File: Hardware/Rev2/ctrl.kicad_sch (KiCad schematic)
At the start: 36 parts, among them J1 USB_C_Receptacle_USB2.0_16P, J2 Conn_01x08, SW1 SW_Push, SW2 SW_Push, U12 74LS125, U13 74LS125, U14 74LS125, U15 ESP32-S3-WROOM-1, U16 USBLC6-2SC6, U17 XC6220B331MR

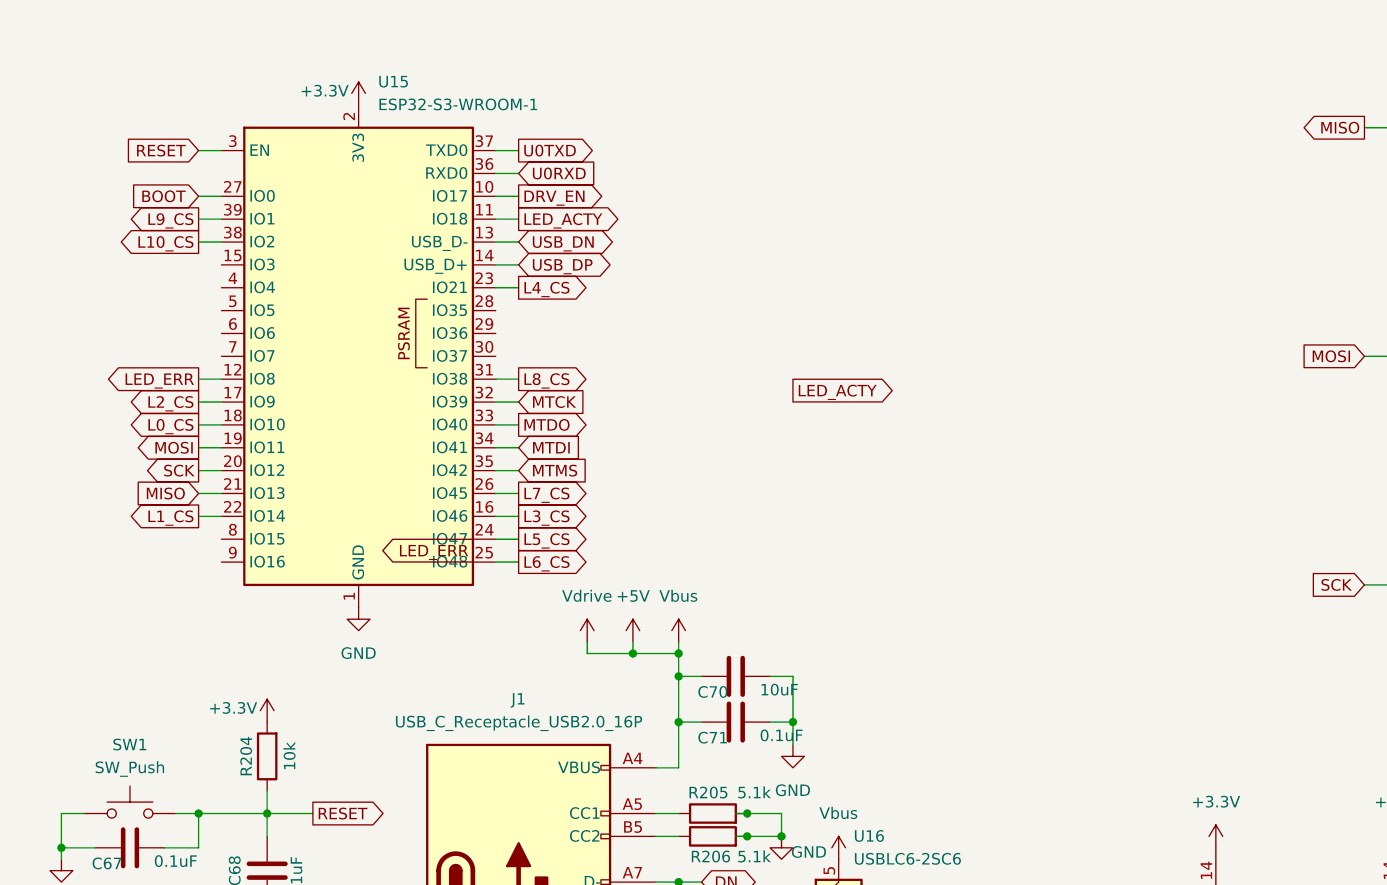
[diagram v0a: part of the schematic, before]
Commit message: add SD card for future expansion
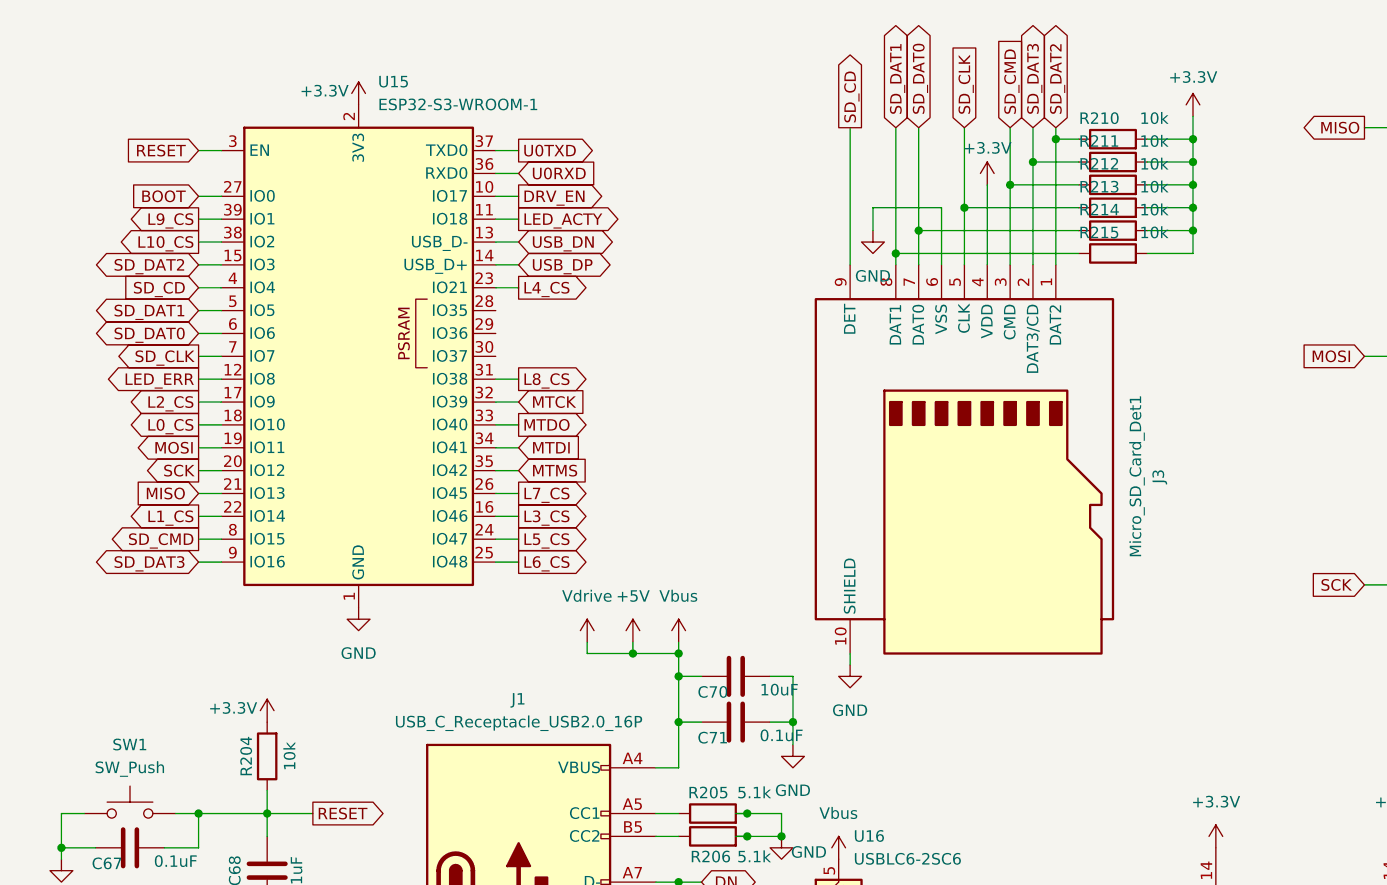
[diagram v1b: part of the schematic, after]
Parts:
- added J3: Micro_SD_Card_Det1, custom_footprints:TFW11-N1S1-2000-A, symbol Connector:Micro_SD_Card_Det1
- added R210, R211, R212, R213, R214, R215: 10k, Resistor_SMD:R_0603_1608Metric_Pad0.98x0.95mm_HandSolder, symbol Device:R
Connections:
- net +3.3V: now also J3.4 (VDD), R210.2, R211.2, R212.2, R213.2, R214.2, R215.2
- net GND: now also J3.10 (SHIELD), J3.6 (VSS)
- net SD_DAT2: now reaches U15.15 (IO3)
- net SD_DAT2: now also J3.1 (DAT2), R210.1
- net SD_CD: now reaches U15.4 (IO4)
- net SD_CD: now also J3.9 (DET)
- net SD_DAT1: now reaches U15.5 (IO5)
- net SD_DAT1: now also J3.8 (DAT1), R215.1
- net SD_DAT0: now reaches U15.6 (IO6)
- net SD_DAT0: now also J3.7 (DAT0), R214.1
- net SD_CLK: now reaches U15.7 (IO7)
- net SD_CLK: now also J3.5 (CLK), R213.1
- net SD_CMD: now reaches U15.8 (IO15)
- net SD_CMD: now also J3.3 (CMD), R212.1
- net SD_DAT3: now reaches U15.9 (IO16)
- net SD_DAT3: now also J3.2 (DAT3/CD), R211.1

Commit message: add power LED
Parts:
- added D736: LED, LED_SMD:LED_1206_3216Metric_Pad1.42x1.75mm_HandSolder, symbol Device:LED
- added R216: 220R, Resistor_SMD:R_0603_1608Metric_Pad0.98x0.95mm_HandSolder, symbol Device:R
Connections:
- net +3.3V: now also R216.1
- net GND: now also D736.1 (K)
- new net: D736.2 (A), R216.2

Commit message: add 3D models, and change USB-C connector type
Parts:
- J1: footprint custom_footprints:TPS16-N1F1-2016-A -> custom_footprints:ShouHan-USBC-16P-2MD; MPN C52750323 -> C2765186
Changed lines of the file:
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@@
 			)
 		)
-		(property "Footprint" "custom_footprints:TPS16-N1F1-2016-A"
+		(property "Footprint" "custom_footprints:ShouHan-USBC-16P-2MD"
 			(at 72.39 111.76 0)
 			(effects
@@
 			)
 		)
-		(property "MPN" "C52750323"
+		(property "MPN" "C2765186"
 			(at 68.58 111.76 0)
 			(effects

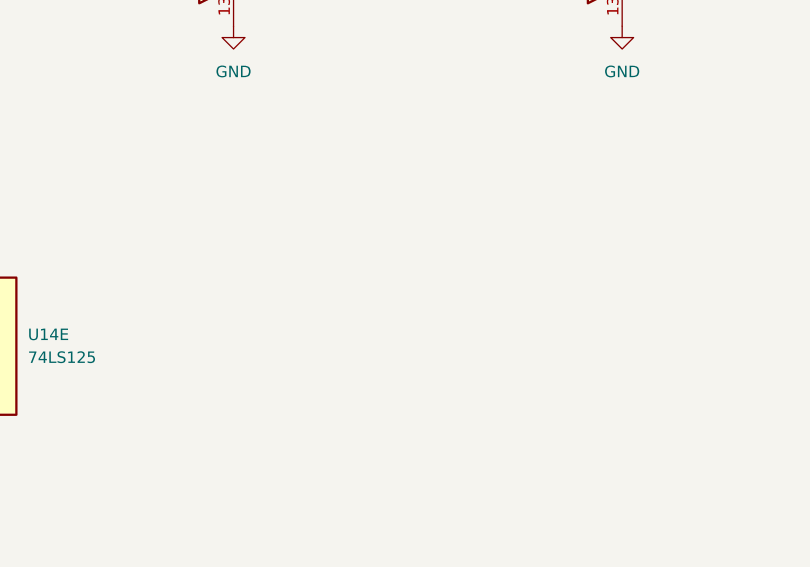
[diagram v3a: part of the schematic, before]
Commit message: add header for SD card pins
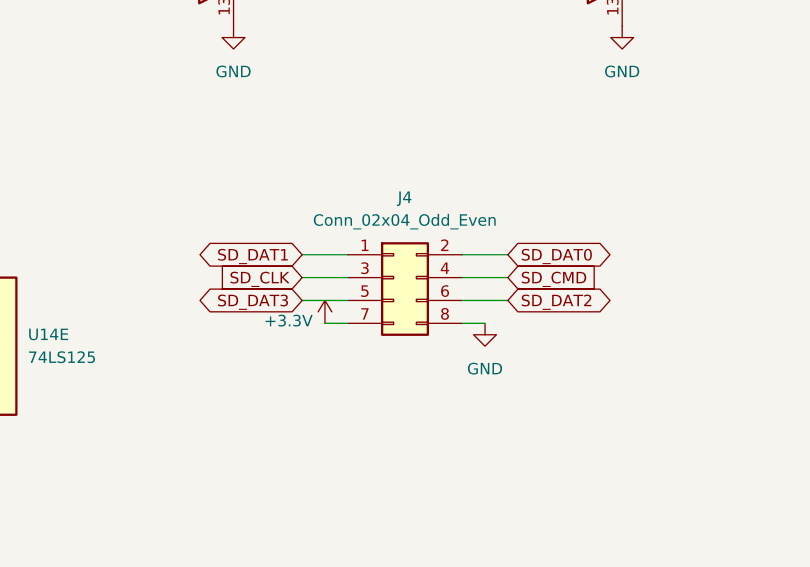
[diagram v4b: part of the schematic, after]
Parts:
- added J4: Conn_02x04_Odd_Even, Connector_PinHeader_2.54mm:PinHeader_2x04_P2.54mm_Vertical, symbol Connector_Generic:Conn_02x04_Odd_Even
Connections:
- net +3.3V: now also J4.7 (Pin_7)
- net GND: now also J4.8 (Pin_8)
- net SD_CLK: now also J4.3 (Pin_3)
- net SD_CMD: now also J4.4 (Pin_4)
- net SD_DAT0: now also J4.2 (Pin_2)
- net SD_DAT1: now also J4.1 (Pin_1)
- net SD_DAT2: now also J4.6 (Pin_6)
- net SD_DAT3: now also J4.5 (Pin_5)

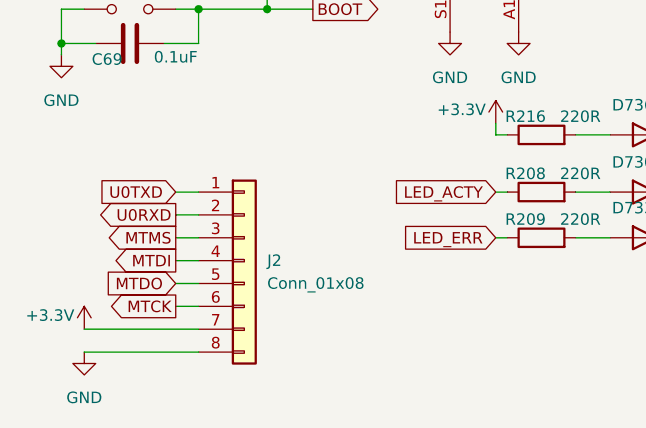
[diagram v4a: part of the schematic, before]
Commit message: add +5V rail to debug header
someone might want to power the board that way :/
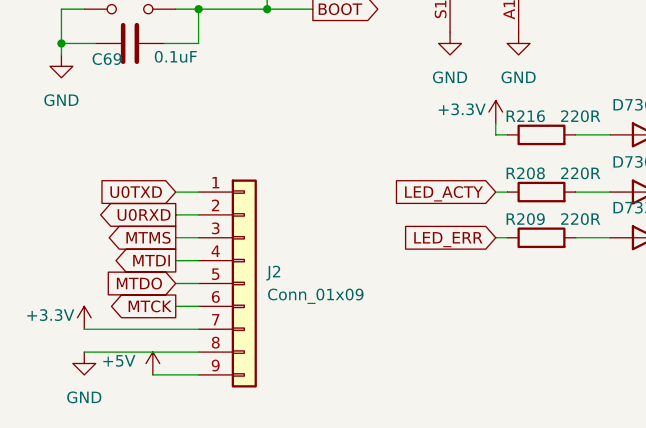
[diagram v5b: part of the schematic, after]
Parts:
- J2: value Conn_01x08 -> Conn_01x09; footprint Connector_PinHeader_2.54mm:PinHeader_1x08_P2.54mm_Vertical -> Connector_PinHeader_2.54mm:PinHeader_1x09_P2.54mm_Vertical; symbol Connector_Generic:Conn_01x08 -> Connector_Generic:Conn_01x09
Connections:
- net +5V: now also J2.9 (Pin_9)
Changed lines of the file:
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@@
 	(wire
 		(pts
-			(xy 180.34 76.2) (xy 181.61 76.2)
+			(xy 30.48 152.4) (xy 33.02 152.4)
 		)
 		(stroke
@@
 	(wire
 		(pts
-			(xy 74.93 157.48) (xy 78.74 157.48)
+			(xy 180.34 76.2) (xy 181.61 76.2)
 		)
 		(stroke
@@
 	(wire
 		(pts
-			(xy 30.48 162.56) (xy 33.02 162.56)
+			(xy 74.93 157.48) (xy 78.74 157.48)
 		)
 		(stroke
@@
 	(wire
 		(pts
-			(xy 30.48 154.94) (xy 33.02 154.94)
+			(xy 33.02 132.08) (xy 30.48 132.08)
 		)
 		(stroke
@@
 	(wire
 		(pts
-			(xy 33.02 132.08) (xy 30.48 132.08)
+			(xy 93.98 101.6) (xy 97.79 101.6)
 		)
 		(stroke
@@
 	(wire
 		(pts
-			(xy 93.98 101.6) (xy 97.79 101.6)
+			(xy 30.48 165.1) (xy 33.02 165.1)
 		)
 		(stroke
@@
 	(wire
 		(pts
+			(xy 30.48 157.48) (xy 33.02 157.48)
+		)
+		(stroke
+			(width 0)
+			(type default)
+		)
+	)
+	(wire
+		(pts
 			(xy 99.06 86.36) (xy 96.52 86.36)
 		)
@@
 	(wire
 		(pts
-			(xy 30.48 157.48) (xy 33.02 157.48)
+			(xy 20.32 132.08) (xy 17.78 132.08)
 		)
 		(stroke
@@
 	(wire
 		(pts
-			(xy 20.32 132.08) (xy 17.78 132.08)
+			(xy 152.4 152.4) (xy 157.48 152.4)
 		)
 		(stroke
@@
 	(wire
 		(pts
-			(xy 152.4 152.4) (xy 157.48 152.4)
+			(xy 223.52 113.03) (xy 228.6 113.03)
 		)
 		(stroke
@@
 	(wire
 		(pts
-			(xy 223.52 113.03) (xy 228.6 113.03)
+			(xy 33.02 38.1) (xy 35.56 38.1)
 		)
 		(stroke
@@
 	(wire
 		(pts
-			(xy 33.02 38.1) (xy 35.56 38.1)
+			(xy 149.86 152.4) (xy 152.4 152.4)
 		)
 		(stroke
@@
 	(wire
 		(pts
-			(xy 149.86 152.4) (xy 152.4 152.4)
+			(xy 20.32 170.18) (xy 33.02 170.18)
 		)
 		(stroke
@@
 	(wire
 		(pts
+			(xy 20.32 167.64) (xy 33.02 167.64)
+		)
+		(stroke
+			(width 0)
+			(type default)
+		)
+	)
+	(wire
+		(pts
 			(xy 138.43 34.29) (xy 143.51 34.29)
 		)
@@
 	(wire
 		(pts
-			(xy 30.48 165.1) (xy 33.02 165.1)
-		)
-		(stroke
-			(width 0)
-			(type default)
-		)
-	)
-	(wire
-		(pts
 			(xy 86.36 109.22) (xy 83.82 109.22)
 		)
@@
 	(wire
 		(pts
-			(xy 162.56 152.4) (xy 167.64 152.4)
+			(xy 27.94 172.72) (xy 33.02 172.72)
 		)
 		(stroke
@@
 	(wire
 		(pts
-			(xy 30.48 152.4) (xy 33.02 152.4)
+			(xy 162.56 152.4) (xy 167.64 152.4)
 		)
 		(stroke
@@
 	(wire
 		(pts
+			(xy 30.48 162.56) (xy 33.02 162.56)
+		)
+		(stroke
+			(width 0)
+			(type default)
+		)
+	)
+	(wire
+		(pts
 			(xy 66.04 55.88) (xy 68.58 55.88)
 		)
@@
 	(wire
 		(pts
-			(xy 20.32 170.18) (xy 33.02 170.18)
-		)
-		(stroke
-			(width 0)
-			(type default)
-		)
-	)
-	(wire
-		(pts
 			(xy 86.36 96.52) (xy 86.36 91.44)
 		)
@@
 	(wire
 		(pts
-			(xy 86.36 109.22) (xy 88.9 109.22)
+			(xy 30.48 160.02) (xy 33.02 160.02)
 		)
 		(stroke
@@
 	(wire
 		(pts
-			(xy 30.48 160.02) (xy 33.02 160.02)
+			(xy 86.36 109.22) (xy 88.9 109.22)
 		)
 		(stroke
@@
 	(wire
 		(pts
-			(xy 20.32 167.64) (xy 33.02 167.64)
-		)
-		(stroke
-			(width 0)
-			(type default)
-		)
-	)
-	(wire
-		(pts
 			(xy 33.02 60.96) (xy 35.56 60.96)
 		)
@@
 	(wire
 		(pts
+			(xy 30.48 154.94) (xy 33.02 154.94)
+		)
+		(stroke
+			(width 0)
+			(type default)
+		)
+	)
+	(wire
+		(pts
 			(xy 33.02 132.08) (xy 40.64 132.08)
 		)
@@
 	)
 	(symbol
-		(lib_id "Connector_Generic:Conn_01x08")
-		(at 38.1 160.02 0)
+		(lib_id "Connector_Generic:Conn_01x09")
+		(at 38.1 162.56 0)
 		(unit 1)
 		(exclude_from_sim no)
@@
 		(fields_autoplaced yes)
 		(property "Reference" "J2"
-			(at 40.64 160.0199 0)
+			(at 40.64 161.2899 0)
 			(effects
 				(font
@@
 			)
 		)
-		(property "Value" "Conn_01x08"
-			(at 40.64 162.5599 0)
+		(property "Value" "Conn_01x09"
+			(at 40.64 163.8299 0)
 			(effects
 				(font
@@
 			)
 		)
-		(property "Footprint" "Connector_PinHeader_2.54mm:PinHeader_1x08_P2.54mm_Vertical"
-			(at 38.1 160.02 0)
+		(property "Footprint" "Connector_PinHeader_2.54mm:PinHeader_1x09_P2.54mm_Vertical"
+			(at 38.1 162.56 0)
 			(effects
 				(font
@@
 		)
 		(property "Datasheet" "~"
-			(at 38.1 160.02 0)
+			(at 38.1 162.56 0)
 			(effects
 				(font
@@
 			)
 		)
-		(property "Description" "Generic connector, single row, 01x08, script generated (kicad-library-utils/schlib/autogen/connector/)"
-			(at 38.1 160.02 0)
+		(property "Description" "Generic connector, single row, 01x09, script generated (kicad-library-utils/schlib/autogen/connector/)"
+			(at 38.1 162.56 0)
 			(effects
 				(font
@@
 		)
 		(property "MPN" "C49451372"
-			(at 38.1 160.02 0)
+			(at 38.1 162.56 0)
 			(effects
 				(font
@@
 		(pin "1"
 		)
+		(pin "9"
+		)
 		(instances
 			(project ""
@@
 					(unit 1)
 				)
+			)
+		)
+	)
+	(symbol
+		(lib_id "power:+3.3V")
+		(at 27.94 172.72 0)
+		(unit 1)
+		(exclude_from_sim no)
+		(in_bom yes)
+		(on_board yes)
+		(dnp no)
+		(property "Reference" "#PWR0114"
+			(at 27.94 176.53 0)
+			(effects
+				(font
+					(size 1.27 1.27)
+				)
+				(hide yes)
+			)
+		)
+		(property "Value" "+5V"
+			(at 24.13 171.196 0)
+			(effects
+				(font
+					(size 1.27 1.27)
+				)
+			)
+		)
+		(property "Footprint" ""
+			(at 27.94 172.72 0)
+			(effects
+				(font
+					(size 1.27 1.27)
+				)
+				(hide yes)
+			)
+		)
+		(property "Datasheet" ""
+			(at 27.94 172.72 0)
+			(effects
+				(font
+					(size 1.27 1.27)
+				)
+				(hide yes)
+			)
+		)
+		(property "Description" "Power symbol creates a global label with name \"+3.3V\""
+			(at 27.94 172.72 0)
+			(effects
+				(font
+					(size 1.27 1.27)
+				)
+				(hide yes)
+			)
+		)
+		(pin "1"
+		)
+		(instances
+			(project "Rev2"
+				(path "/179c1fb3-28fd-4881-8d54-9aff58c09fe4/a439bf26-855a-431e-bb37-b656be58d856"
+					(reference "#PWR0114")
+					(unit 1)
+				)

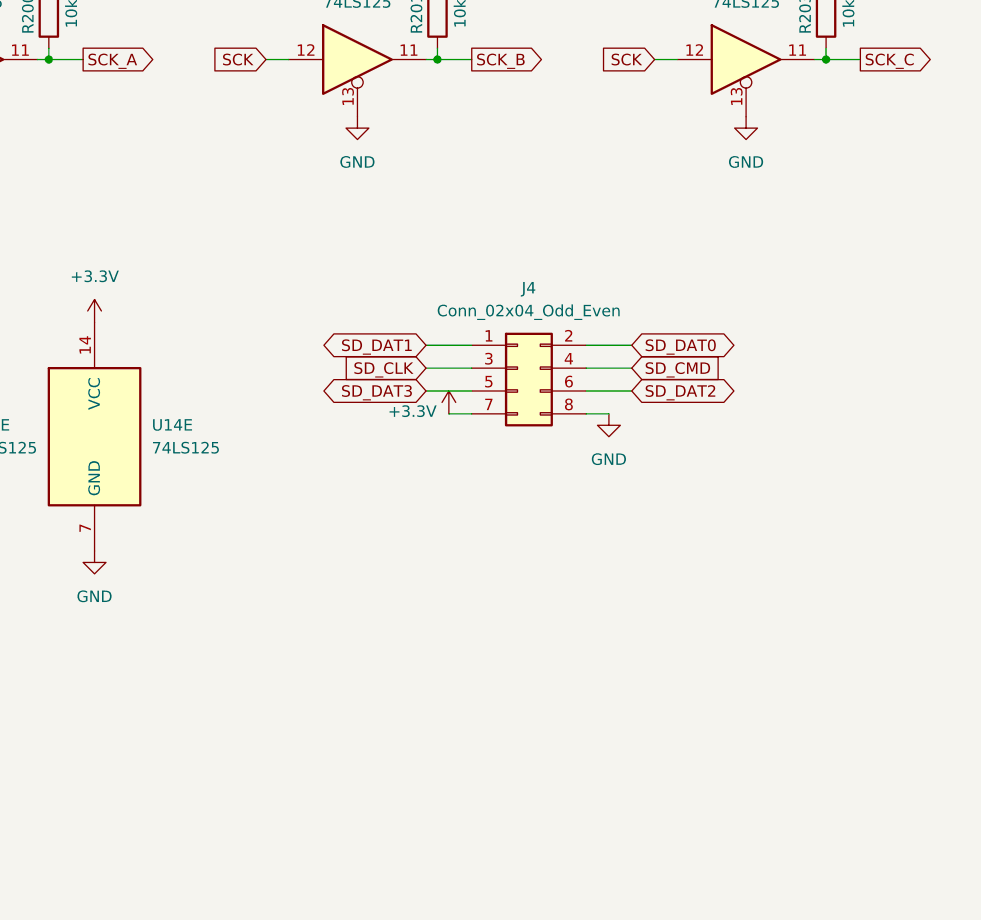
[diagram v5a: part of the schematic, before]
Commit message: add OLED display
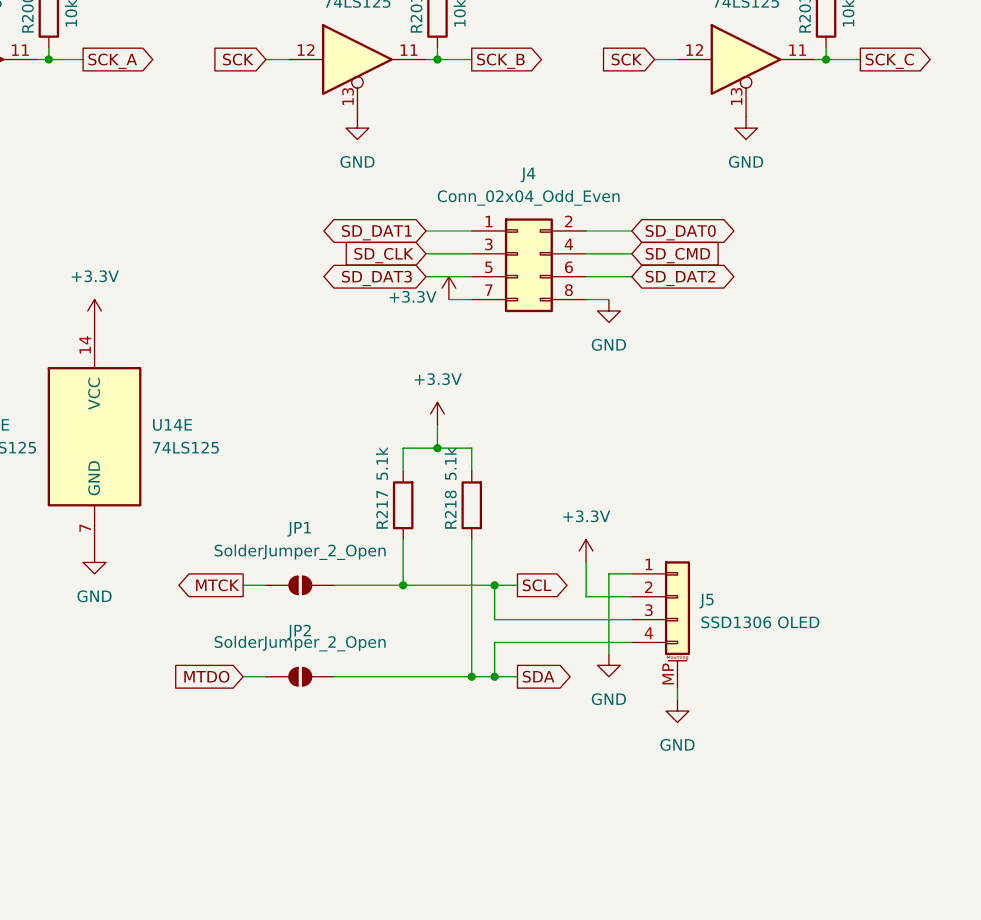
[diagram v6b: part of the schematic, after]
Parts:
- added J5: SSD1306 OLED, custom_footprints:HS96L03W2C03, symbol Connector_Generic_MountingPin:Conn_01x04_MountingPin
- added JP1, JP2: SolderJumper_2_Open, Jumper:SolderJumper-2_P1.3mm_Open_TrianglePad1.0x1.5mm, symbol Jumper:SolderJumper_2_Open
- added R217, R218: 5.1k, Resistor_SMD:R_0603_1608Metric_Pad0.98x0.95mm_HandSolder, symbol Device:R
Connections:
- net +3.3V: now also J5.2 (Pin_2), R217.2, R218.2
- net GND: now also J5.1 (Pin_1), J5.MP (MountPin)
- net MTCK: now also JP1.1 (A)
- net MTDO: now also JP2.1 (A)
- new net SCL: J5.3 (Pin_3), JP1.2 (B), R217.1
- new net SDA: J5.4 (Pin_4), JP2.2 (B), R218.1
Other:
- moved on the sheet: J4
